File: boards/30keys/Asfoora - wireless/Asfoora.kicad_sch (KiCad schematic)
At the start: 75 parts, among them SW10 SW_Push, SW11 SW_Push, SW12 SW_Push, SW13 SW_Push, SW14 SW_Push, SW15 SW_Push, SW17 SW_Push, SW18 SW_Push, SW19 SW_Push, SW2 SW_Push, SW20 SW_Push, SW21 SW_Push, SW22 SW_Push, SW23 SW_Push, SW24 SW_Push, SW25 SW_Push, SW26 SW_Push, SW27 SW_Push, SW28 SW_Push, SW29 SW_Push, SW3 SW_Push, SW30 SW_Push, SW31 SW_Push, SW32 SW_Push, SW33 SW_Push, SW34 SW_SPDT, SW4 SW_Push, SW5 SW_Push, SW6 SW_Push, SW7 SW_Push, SW8 SW_Push, SW9 SW_Push, U1 ProMicro_r

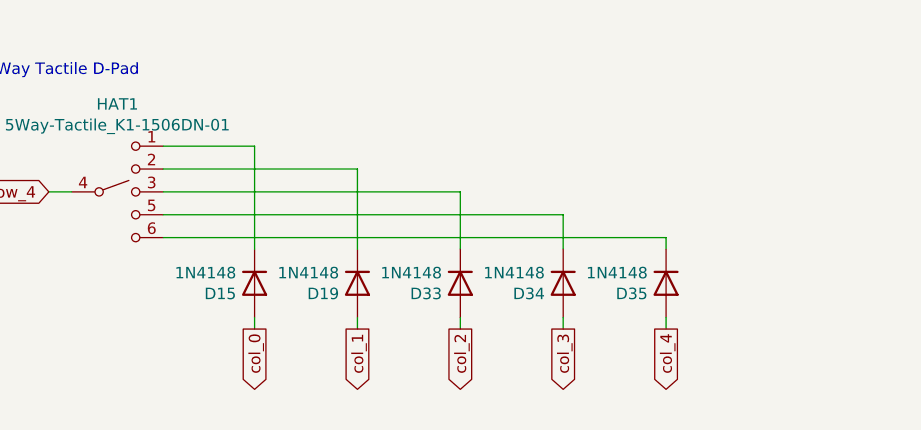
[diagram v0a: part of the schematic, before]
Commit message: fix 5 way switch on wasfoora
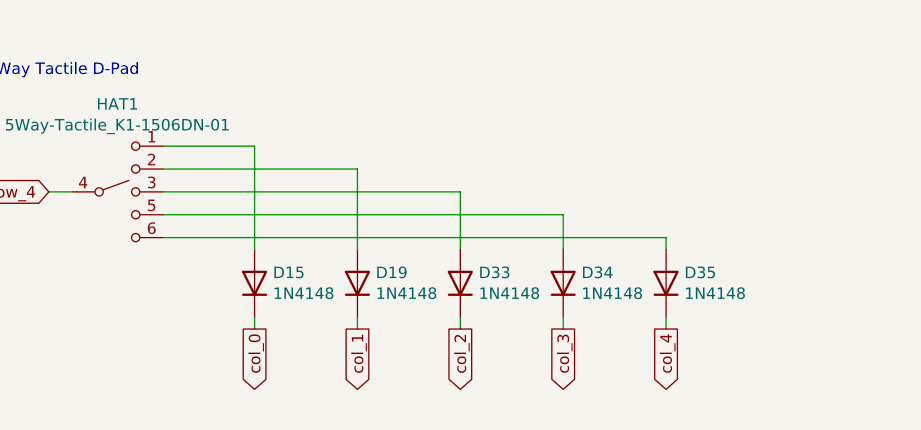
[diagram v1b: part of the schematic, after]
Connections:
- net col_0: now also D15.1 (K); no longer D15.2 (A)
- net col_1: now also D19.1 (K); no longer D19.2 (A)
- net col_2: now also D33.1 (K); no longer D33.2 (A)
- net col_3: now also D34.1 (K); no longer D34.2 (A)
- net col_4: now also D35.1 (K); no longer D35.2 (A)
- net at HAT1.6: now also D35.2 (A); no longer D35.1 (K)
- net at HAT1.3: now also D33.2 (A); no longer D33.1 (K)
- net at HAT1.5: now also D34.2 (A); no longer D34.1 (K)
- net at HAT1.2: now also D19.2 (A); no longer D19.1 (K)
- net at HAT1.1: now also D15.2 (A); no longer D15.1 (K)
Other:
- moved on the sheet: D15, D19, D33, D34, D35
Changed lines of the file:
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@@
     )
   )
-  (symbol (lib_id "Device:D") (at 134.62 171.45 270) (unit 1)
+  (symbol (lib_id "Device:D") (at 134.62 171.45 90) (unit 1)
     (in_bom yes) (on_board yes) (dnp no)
-    (property "Reference" "D35" (at 132.588 172.6184 90)
-      (effects (font (size 1.27 1.27)) (justify right))
-    )
-    (property "Value" "1N4148" (at 132.588 170.307 90)
+    (property "Reference" "D35" (at 136.652 170.2816 90)
+      (effects (font (size 1.27 1.27)) (justify right))
+    )
+    (property "Value" "1N4148" (at 136.652 172.593 90)
       (effects (font (size 1.27 1.27)) (justify right))
     )
@@
     )
   )
-  (symbol (lib_id "Device:D") (at 111.76 171.45 270) (unit 1)
+  (symbol (lib_id "Device:D") (at 111.76 171.45 90) (unit 1)
     (in_bom yes) (on_board yes) (dnp no)
-    (property "Reference" "D33" (at 109.728 172.6184 90)
-      (effects (font (size 1.27 1.27)) (justify right))
-    )
-    (property "Value" "1N4148" (at 109.728 170.307 90)
+    (property "Reference" "D33" (at 113.792 170.2816 90)
+      (effects (font (size 1.27 1.27)) (justify right))
+    )
+    (property "Value" "1N4148" (at 113.792 172.593 90)
       (effects (font (size 1.27 1.27)) (justify right))
     )
@@
     )
   )
-  (symbol (lib_id "Device:D") (at 123.19 171.45 270) (unit 1)
+  (symbol (lib_id "Device:D") (at 123.19 171.45 90) (unit 1)
     (in_bom yes) (on_board yes) (dnp no)
-    (property "Reference" "D34" (at 121.158 172.6184 90)
-      (effects (font (size 1.27 1.27)) (justify right))
-    )
-    (property "Value" "1N4148" (at 121.158 170.307 90)
+    (property "Reference" "D34" (at 125.222 170.2816 90)
+      (effects (font (size 1.27 1.27)) (justify right))
+    )
+    (property "Value" "1N4148" (at 125.222 172.593 90)
       (effects (font (size 1.27 1.27)) (justify right))
     )
@@
     )
   )
-  (symbol (lib_id "Device:D") (at 100.33 171.45 270) (unit 1)
+  (symbol (lib_id "Device:D") (at 100.33 171.45 90) (unit 1)
     (in_bom yes) (on_board yes) (dnp no)
-    (property "Reference" "D19" (at 98.298 172.6184 90)
-      (effects (font (size 1.27 1.27)) (justify right))
-    )
-    (property "Value" "1N4148" (at 98.298 170.307 90)
+    (property "Reference" "D19" (at 102.362 170.2816 90)
+      (effects (font (size 1.27 1.27)) (justify right))
+    )
+    (property "Value" "1N4148" (at 102.362 172.593 90)
       (effects (font (size 1.27 1.27)) (justify right))
     )
@@
     )
   )
-  (symbol (lib_id "Device:D") (at 88.9 171.45 270) (unit 1)
+  (symbol (lib_id "Device:D") (at 88.9 171.45 90) (unit 1)
     (in_bom yes) (on_board yes) (dnp no)
-    (property "Reference" "D15" (at 86.868 172.6184 90)
-      (effects (font (size 1.27 1.27)) (justify right))
-    )
-    (property "Value" "1N4148" (at 86.868 170.307 90)
-      (effects (font (size 1.27 1.27)) (justify right))
-    )
+    (property "Reference" "D15" (at 90.932 170.2816 90)
+      (effects (font (size 1.27 1.27)) (justify right))
+    )
+    (property "Value" "1N4148" (at 90.932 172.593 90)
+      (effects (font (size 1.27 1.27)) (justify right))
+    )
